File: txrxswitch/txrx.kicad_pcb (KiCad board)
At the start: 2 copper layers, 25 x 25 mm, 33 parts, among them J101 SMA, J102 SMA, J103 SMA, P101 CONN_01X02, T101 MOSN_SMALL, T102 MOSN_SMALL, T103 MOSP_SMALL, T104 MOSP_SMALL, U101 MMIC_SMALL, U102 PGA-103+

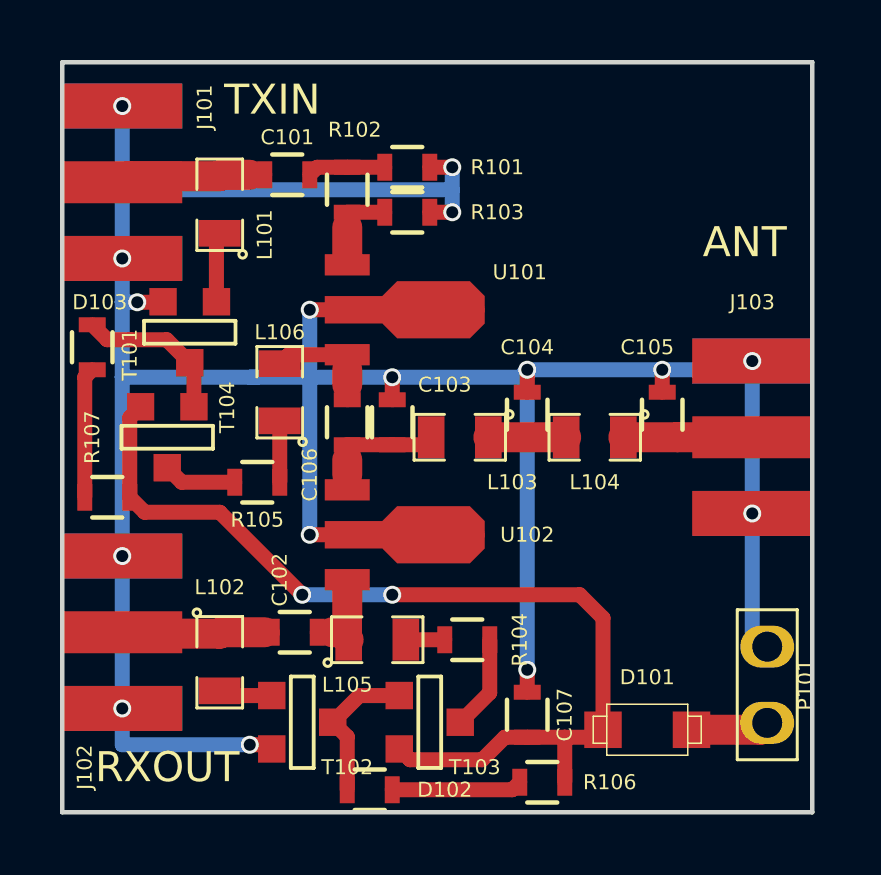
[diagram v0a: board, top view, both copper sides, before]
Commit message: tx/rx switch complete
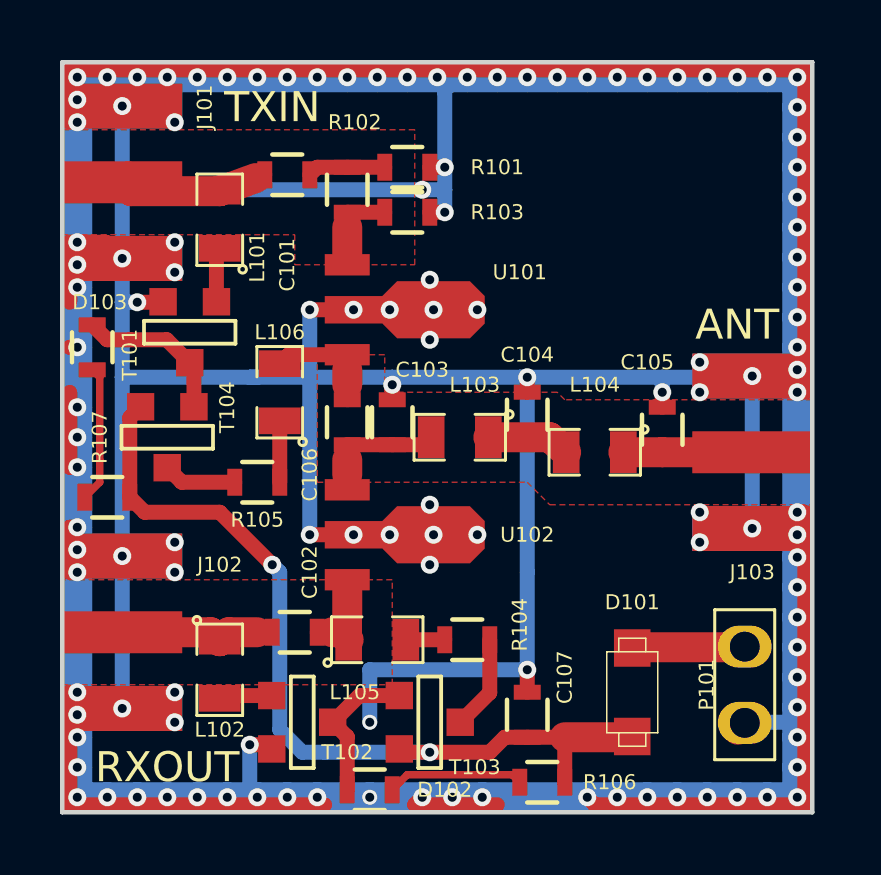
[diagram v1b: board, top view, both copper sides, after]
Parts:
- moved D101 1.35 mm to (35.0, 38.0), turned to 270 degrees
- moved P101 0.75 mm to (38.8, 37.8), turned to 270 degrees
- moved C105 0.50 mm to (36.0, 29.2)
- moved J103 0.50 mm to (39.0, 30.0)
- moved L101 0.50 mm to (21.2, 22.2)
- moved L104 0.50 mm to (33.8, 30.0)
- moved L102 0.25 mm to (21.2, 37.2)
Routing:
- net GND: track 105.7 -> 343.7 mm, vias 16 -> 124
- net VDD: track 33.2 -> 29.4 mm
- net Net-(D101-PadA): track 2.62 -> 3.78 mm
- net Net-(D102-Pad1): track 4.35 -> 4.91 mm
- net Net-(C105-Pad2): track 4.80 -> 4.30 mm
- added copper zone on B.Cu, net GND
- added copper zone on F.Cu, net GND
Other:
- net class Default: via_drill 0.4 -> 0.3
- board text added: "FROM TX"
- board text added: "TO RX"
